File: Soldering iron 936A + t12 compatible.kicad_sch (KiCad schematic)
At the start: 72 parts, among them J1 DC INPUT, J2 OLED, J3 AC input, J4 output_connector, J5 mosfet_driver_future_backup, J6 OLED, Q1 IRF9540N, Q2 BC547, SW1 RotaryEncoder_Switch, U1 LM2596S-ADJ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

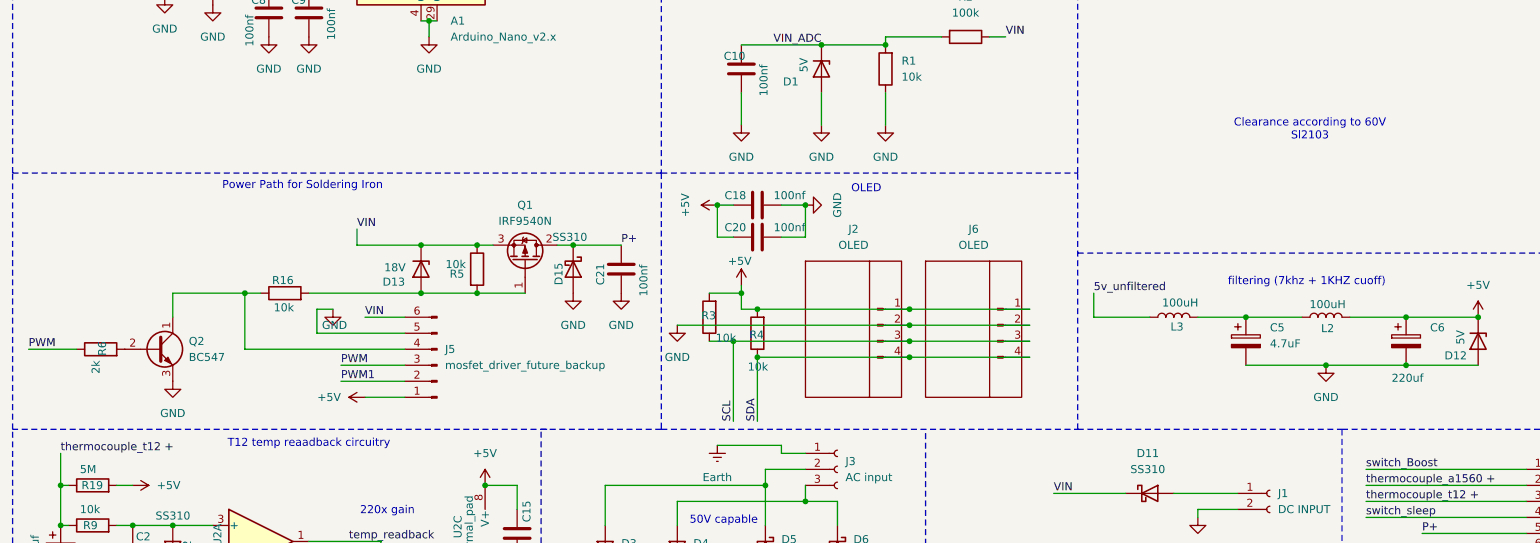
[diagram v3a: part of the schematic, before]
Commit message: Schematic finalised -> will do layout next
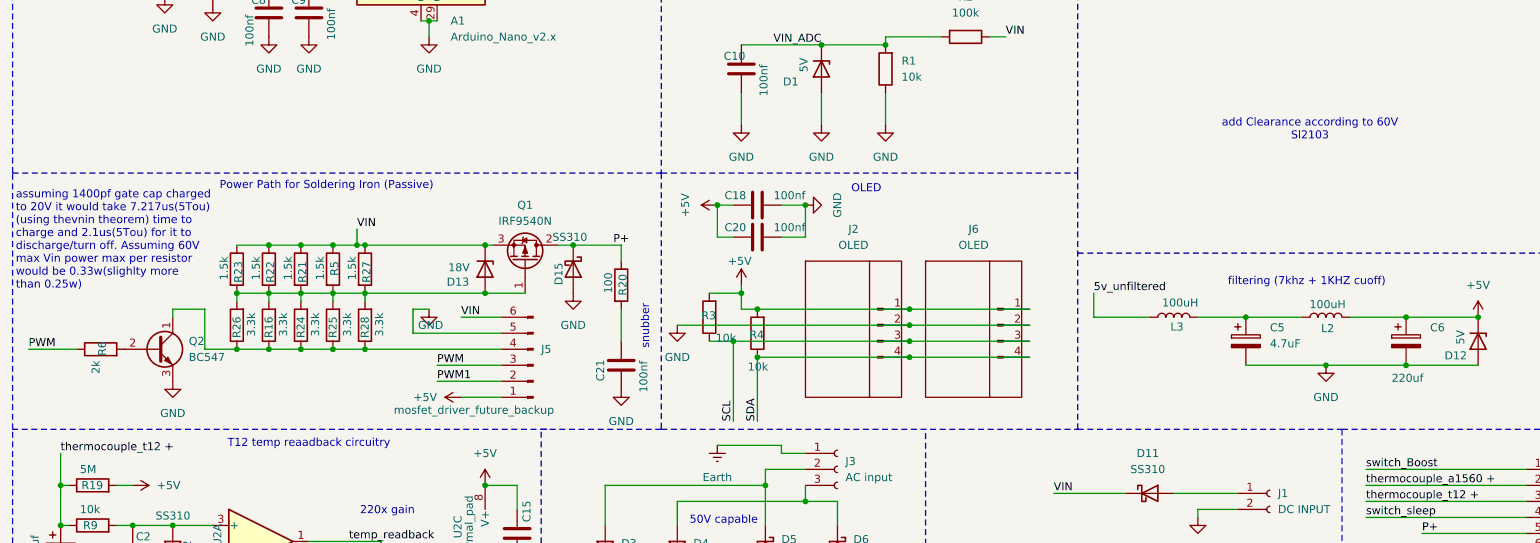
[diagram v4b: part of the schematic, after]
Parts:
- added R20: 100, Resistor_SMD:R_1206_3216Metric_Pad1.30x1.75mm_HandSolder, symbol Device:R
- added R21, R22, R23, R27: 1.5k, Resistor_SMD:R_1206_3216Metric_Pad1.30x1.75mm_HandSolder, symbol Device:R
- added R24, R25, R26, R28: 3.3k, Resistor_SMD:R_1206_3216Metric_Pad1.30x1.75mm_HandSolder, symbol Device:R
- R16: value 10k -> 3.3k
- R5: value 10k -> 1.5k
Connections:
- net P+: now also R20.1; no longer C21.1
- net VIN: now also R21.1, R22.1, R23.1, R27.1
- net at J5.4 (Pin_4), Q2.1 (C), R16.1: now also R24.1, R25.1, R26.1, R28.1
- net at D13.2 (A), Q1.1 (G), R16.2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: now also R21.2, R22.2, R23.2, R24.2, R25.2, R26.2, R27.2, R28.2
- new net: C21.1, R20.2
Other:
- note added: "Power Path for Soldering Iron (Passive)"
- note added: "add Clearance according to 60V Sl2103"
- note added: "assuming 1400pf gate cap charged to 20V it would take 7.217us(5Tou) (using thevnin theorem) time to charge and 2.1us(5Tou) for it to discharge/turn off. Assuming 60V max Vin power max per resistor would be 0.33w(slighlty more than 0.25w)"
- note added: "snubber"
- note removed: "Clearance according to 60V Sl2103"
- note removed: "Power Path for Soldering Iron"
- moved on the sheet: C21, D13, J5, R16, R5

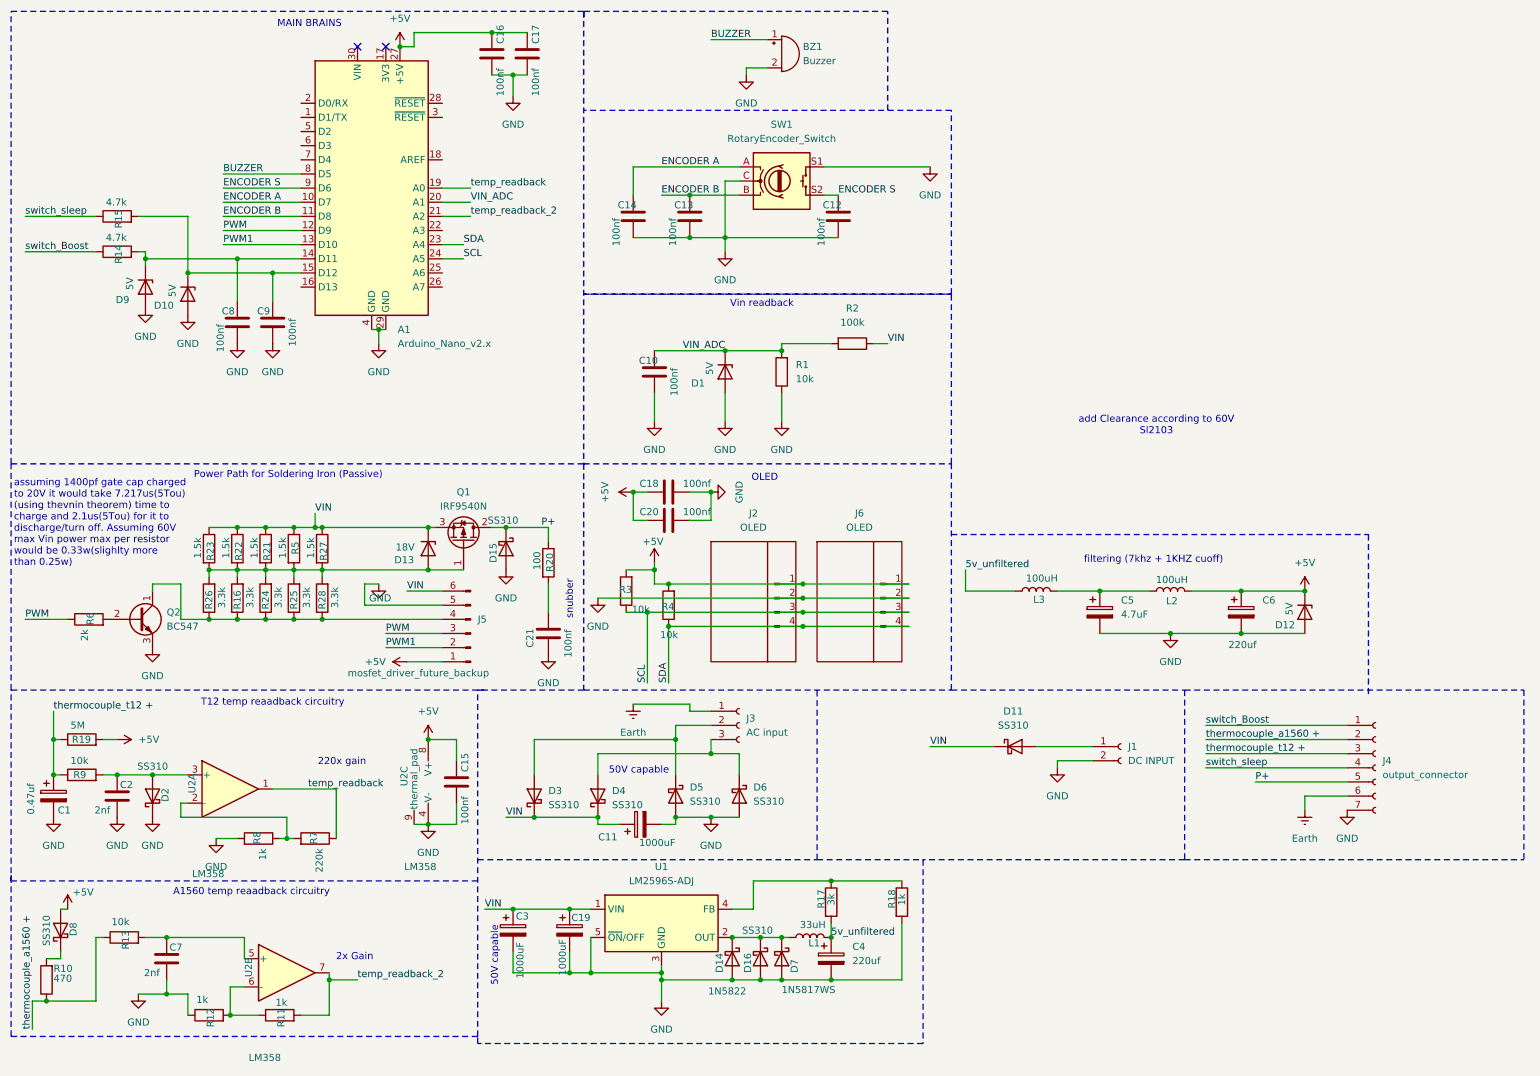
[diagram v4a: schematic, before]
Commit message: added all 3d model files , almost finalised schematic , rough placment of big components
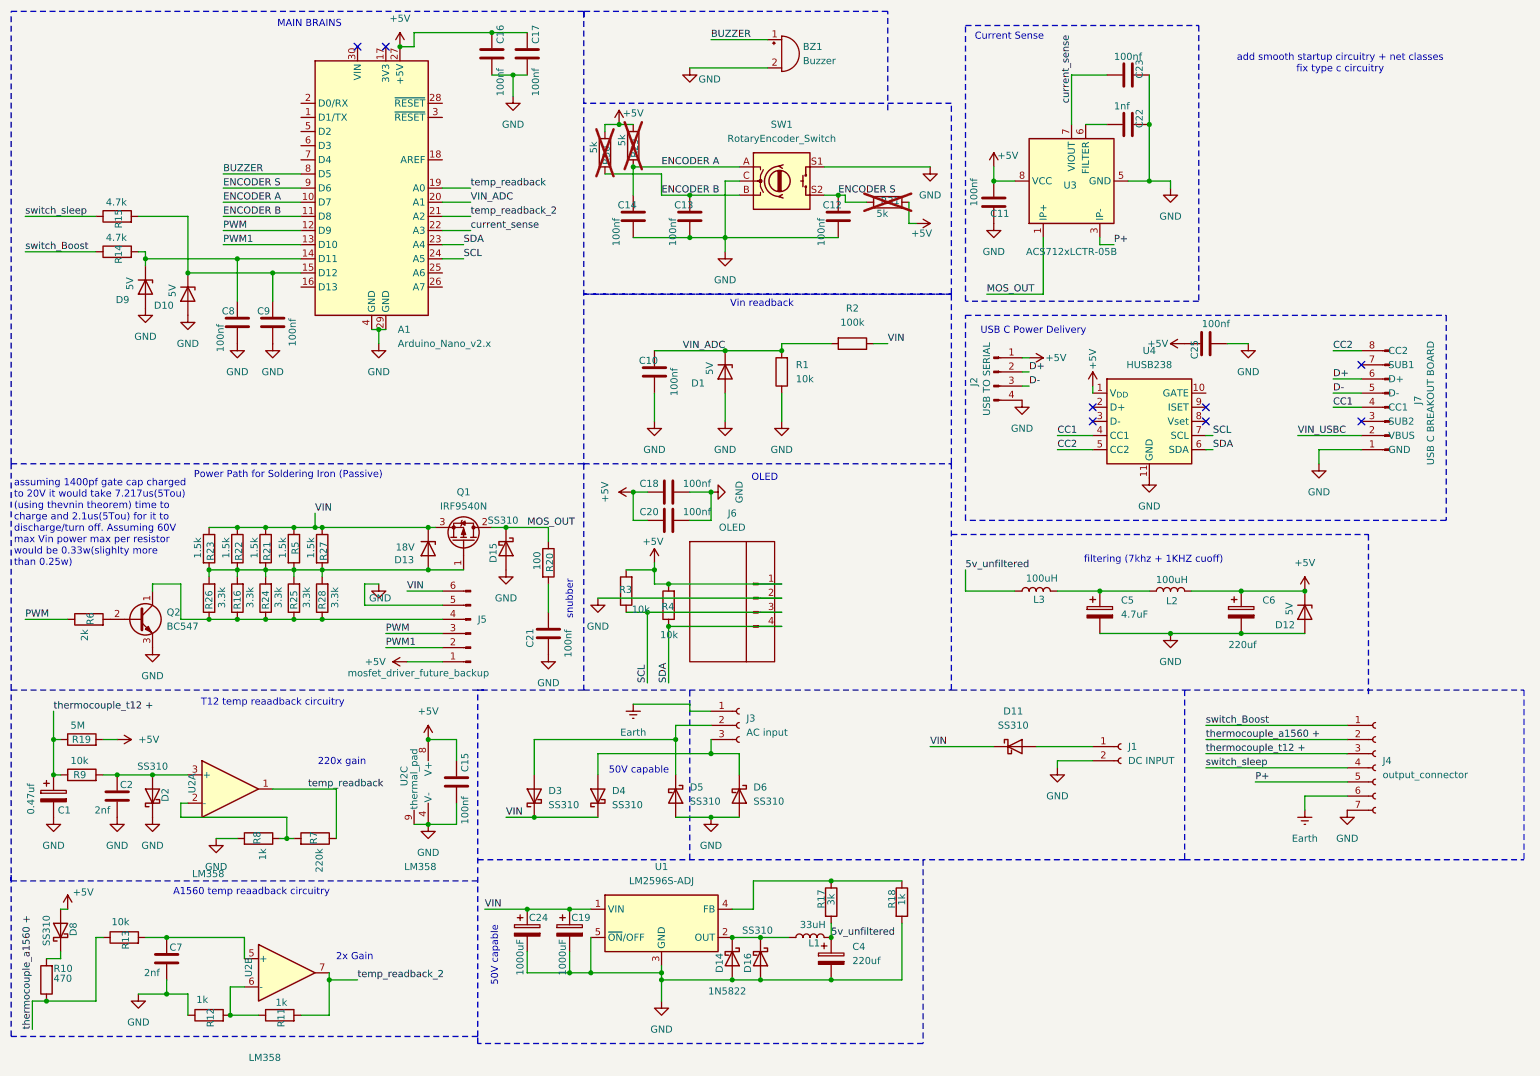
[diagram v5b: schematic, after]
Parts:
- removed C11, C3: 1000uF, Capacitor_THT:CP_Radial_D16.0mm_P7.50mm, symbol Device:C_Polarized
- removed D7: 1N5817WS, Diode_SMD:D_SOD-323, symbol Diode:1N5819WS
- added C11, C23, C25: 100nf, Capacitor_SMD:C_0603_1608Metric_Pad1.08x0.95mm_HandSolder, symbol Device:C
- added C22: 1nf, Capacitor_SMD:C_0603_1608Metric_Pad1.08x0.95mm_HandSolder, symbol Device:C
- added C24: 1000uF, Capacitor_THT:CP_Radial_D16.0mm_P7.50mm, symbol Device:C_Polarized
- added J7: USB C BREAKOUT BOARD, symbol Connector:Conn_01x08_Pin
- added R29, R30, R31: 5k, Resistor_SMD:R_1206_3216Metric_Pad1.30x1.75mm_HandSolder, symbol Device:R
- added U3: ACS712xLCTR-05B, Package_SO:SOIC-8_3.9x4.9mm_P1.27mm, symbol Sensor_Current:ACS712xLCTR-05B
- added U4: HUSB238, Package_DFN_QFN:DFN-10-1EP_3x3mm_P0.5mm_EP1.58x2.35mm, symbol Battery_Management:MCP73833-xxx-MF
- J2: value OLED -> USB TO SERIAL; footprint Connector_PinHeader_2.54mm:PinHeader_1x04_P2.54mm_Vertical -> (none)
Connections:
- net +5V: now also C11.2, C25.1, R29.1, R30.1, R31.2, U3.8 (VCC), U4.1 (V_{DD}), U4.2 (D+)
- net ENCODER A: now also R29.2
- net ENCODER B: now also R30.2
- net ENCODER S: now also R31.1
- net GND: now also J2.4 (Pin_4), C11.1, C22.1, C23.1, C24.2, C25.2, J7.1 (GND), U3.5 (GND), U4.11 (GND); no longer J2.2 (SCL)
- net P+: now also U3.3 (IP-), U3.4 (IP-); no longer D15.1 (K), Q1.2 (D), R20.1
- net SCL: now also U4.7 (SCL); no longer J2.3 (GND)
- net SDA: now also U4.6 (SDA); no longer J2.4 (VDD)
- net VIN: now also C24.1
- net current_sense: now reaches A1.22 (A3)
- net current_sense: now also C23.2, U3.7 (VIOUT)
- new net: C22.2, U3.6 (FILTER)
- new net CC1: J7.4 (CC1), U4.4 (CC1)
- new net CC2: J7.8 (CC2), U4.5 (CC2)
- new net D+: J2.2 (Pin_2), J7.6 (D+)
- new net D-: J2.3 (Pin_3), J7.5 (D-)
- new net MOS_OUT: D15.1 (K), Q1.2 (D), R20.1, U3.1 (IP+), U3.2 (IP+)
- new net VIN_USBC: J7.2 (VBUS)
- no-connect marks 2 -> 8
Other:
- note added: "Current Sense"
- note added: "USB C Power Delivery"
- note added: "add smooth startup circuitry + net classes fix type c circuitry"
- note removed: "add Clearance according to 60V Sl2103"
- moved on the sheet: J6

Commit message: Finalised schematic , placement
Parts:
- added 5V1, GND1, PWM1, SCL1, SDA1, VBUS1: TestPoint, TestPoint:TestPoint_Pad_D1.0mm, symbol Connector:TestPoint
- added C26: 1uF, Capacitor_SMD:C_0603_1608Metric_Pad1.08x0.95mm_HandSolder, symbol Device:C
- added D17, D18, D19, D7: SS310, Diode_SMD:D_SMA, symbol Diode:SS310
- added F1: Fuse, Fuse:Fuse_1206_3216Metric_Pad1.42x1.75mm_HandSolder, symbol Device:Fuse
- added R32: 22.6K, Resistor_SMD:R_1206_3216Metric_Pad1.30x1.75mm_HandSolder, symbol Device:R
- added R33: 10k, Resistor_SMD:R_1206_3216Metric_Pad1.30x1.75mm_HandSolder, symbol Device:R
- added R34, R38: 5.1K, Resistor_SMD:R_1206_3216Metric_Pad1.30x1.75mm_HandSolder, symbol Device:R
- added R35: 1M, Resistor_SMD:R_1206_3216Metric_Pad1.30x1.75mm_HandSolder, symbol Device:R
- added R36: 50K, Resistor_SMD:R_1206_3216Metric_Pad1.30x1.75mm_HandSolder, symbol Device:R
- added R37: 10K, Resistor_SMD:R_1206_3216Metric_Pad1.30x1.75mm_HandSolder, symbol Device:R
- added U5: PC817, Package_DIP:DIP-4_W7.62mm, symbol Isolator:PC817
- D13: footprint Diode_THT:D_A-405_P10.16mm_Horizontal -> Diode_THT:D_A-405_P2.54mm_Vertical_KathodeUp
- J2: footprint (none) -> Connector_PinHeader_2.54mm:PinHeader_1x04_P2.54mm_Vertical
- J7: footprint (none) -> Connector_PinHeader_2.54mm:PinHeader_1x08_P2.54mm_Vertical
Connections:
- net +5V: now also 5V1.1, D7.2 (A), R37.2; no longer U4.1 (V_{DD}), U4.2 (D+)
- net CC1: now also R38.2
- net CC2: now also R34.2
- net Earth: now also F1.1, R35.2, R36.2; no longer J4.6 (Pin_6)
- net GND: now also C26.2, GND1.1, R32.2, R33.2, R34.1, R38.1, U5.3
- net MOS_OUT: now also U3.3 (IP-), U3.4 (IP-); no longer U3.1 (IP+), U3.2 (IP+)
- net P+: now also U3.1 (IP+), U3.2 (IP+); no longer U3.3 (IP-), U3.4 (IP-)
- net PWM: now also PWM1.1
- net SCL: now also SCL1.1
- net SDA: now also SDA1.1
- net VIN: now also D19.1 (K)
- net VIN_USBC: now also D17.2 (A), D19.2 (A), VBUS1.1
- net LEAK_ERR: now reaches A1.7 (D4)
- net LEAK_ERR: now also R37.1, U5.4
- net at U4.8 (Vset): now also R33.1
- net at U4.9 (ISET): now also R32.1
- new net: D18.2 (A), F1.2, J4.6 (Pin_6), R35.1, U5.2
- new net: D18.1 (K), R36.1, U5.1
- new net: C26.1, D17.1 (K), D7.1 (K), U4.1 (V_{DD}), U4.2 (D+)
- no-connect marks 8 -> 6
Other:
- note added: "NORMAL POWER INPUT"
- note added: "OUTPUT"
- note added: "add smooth startup circuitry + net classes"
- note added: "if the soldering ironis touched onto a live circuit somehow then the fuse would blow and if still the iron is held/touched at the source then the optotcoupler will light up and signal Arduino to shut down"
- note added: "iron Current Sense"
- note removed: "Current Sense"
- note removed: "add smooth startup circuitry + net classes fix type c circuitry"
- moved on the sheet: C25, C5, C6, D11, D12, J1, J2, J4, J7, L2, L3, U4

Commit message: Almost completed layout , checks pending
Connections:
- net at C26.1, D17.1 (K), D7.1 (K)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: no longer U4.2 (D+)
- no-connect marks 6 -> 4
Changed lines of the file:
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@@
 	)
 	(junction
+		(at 118.11 147.32)
+		(diameter 0)
+		(color 0 0 0 0)
+	)
+	(junction
 		(at 17.78 121.92)
 		(diameter 0)
@@
 	)
 	(no_connect
-		(at 220.98 147.32)
-	)
-	(no_connect
 		(at 269.24 147.32)
 	)
@@
 		(at 269.24 137.16)
 	)
-	(no_connect
-		(at 220.98 144.78)
-	)
 	(wire
 		(pts
@@
 		)
 	)
+	(wire
+		(pts
+			(xy 118.11 147.32) (xy 118.11 146.05)
+		)
+		(stroke
+			(width 0)
+			(type default)
+		)
+	)
 	(polyline
 		(pts
@@
 	(wire
 		(pts
-			(xy 118.11 149.86) (xy 118.11 146.05)
+			(xy 118.11 149.86) (xy 118.11 147.32)
 		)
 		(stroke
@@
 	(wire
 		(pts
+			(xy 116.84 147.32) (xy 118.11 147.32)
+		)
+		(stroke
+			(width 0)
+			(type default)
+		)
+	)
+	(wire
+		(pts
 			(xy 67.31 102.87) (xy 67.31 105.41)
 		)
@@
 		)
 	)
+	(netclass_flag ""
+		(length 2.54)
+		(shape round)
+		(at 116.84 147.32 90)
+		(fields_autoplaced yes)
+		(effects
+			(font
+				(size 1.27 1.27)
+			)
+			(justify left bottom)
+		)
+		(property "Netclass" "Power_60V"
+			(at 114.3 146.6215 90)
+			(effects
+				(font
+					(size 1.27 1.27)
+				)
+				(justify left)
+				(hide yes)
+			)
+		)
+		(property "Component Class" ""
+			(at -58.42 2.54 0)
+			(effects
+				(font
+					(size 1.27 1.27)
+					(italic yes)
+				)
+			)
+		)
+	)
+	(netclass_flag ""
+		(length 2.54)
+		(shape round)
+		(at 106.68 143.51 0)
+		(fields_autoplaced yes)
+		(effects
+			(font
+				(size 1.27 1.27)
+			)
+			(justify left bottom)
+		)
+		(property "Netclass" "Power_60V"
+			(at 107.3785 140.97 0)
+			(effects
+				(font
+					(size 1.27 1.27)
+				)
+				(justify left)
+				(hide yes)
+			)
+		)
+		(property "Component Class" ""
+			(at -68.58 -1.27 0)
+			(effects
+				(font
+					(size 1.27 1.27)
+					(italic yes)
+				)
+			)
+		)
+	)
 	(symbol
 		(lib_id "Device:R")
@@
 		(pin "6"
 		)
-		(pin "10"
-		)
 		(pin "2"
 		)
@@
 		(pin "4"
 		)
-		(pin "2"
-		)
 		(pin "11"
